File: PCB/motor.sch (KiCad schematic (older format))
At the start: 18 parts, among them J20 70543-0003, U5 TMC2130-TA

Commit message: Change 1k resistors to 4.7k. Update Symbols
Had to update the symbols to the right library again, since
Kicad Nightly changed their library order.

Also changed the 1k resistors to 4.7k to unify resistors and
also upped the PU to a weaker value.
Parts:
- C45, C46, C47, C48, C49, C50, C52, C53: symbol remram-rescue:C-Device -> Device:C
- C51: symbol remram-rescue:CP-Device -> Device:CP
- R37, R38, R39: symbol remram-rescue:R-Device -> Device:R
- TP20, TP21, TP22, TP23: symbol remram-rescue:Test_Point-Connector_Specialized -> Connector:Test_Point

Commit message: Added protection diodes to TMC2130
Diode on IO voltage protects chip to only accept command when
motor voltage is present.

Clamping diodes on motor outputs are for inductive loads.
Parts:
- added D32, D33, D34, D35, D36, D37, D38, D39, D40: S310FA, Diode_SMD:D_SOD-123, symbol Device:D_Schottky
- added R38: 10k, Resistor_SMD:R_0603_1608Metric, symbol Device:R
- renumbered R38 to R39, R39 to R40
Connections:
- net labels added: GND
- wire segments 43 -> 76
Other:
- moved on the sheet: J20, R39

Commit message: Rework the PCB after feedback
This design incooperated following changes:
 * Better power distribution
 * Diodes for driver, endstops and fan tachometer
 * Mounting holes not grounded and size 3.5mm
 * Better EXT3 header description
 * EXT1 and EXT2 footprint for normal 2.54 header
 * Reverse voltage protection for the battery
 * PU for driver enable pin
 * Better crystal placement
 * 2 sided board layout for better routing and
   placement
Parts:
- removed TP20: OA1, TestPoint:TestPoint_Pad_D1.0mm, symbol Connector:Test_Point
- removed TP21: OA2, TestPoint:TestPoint_Pad_D1.0mm, symbol Connector:Test_Point
- removed TP22: OB2, TestPoint:TestPoint_Pad_D1.0mm, symbol Connector:Test_Point
- removed TP23: OB1, TestPoint:TestPoint_Pad_D1.0mm, symbol Connector:Test_Point
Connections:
- wire segments 76 -> 68

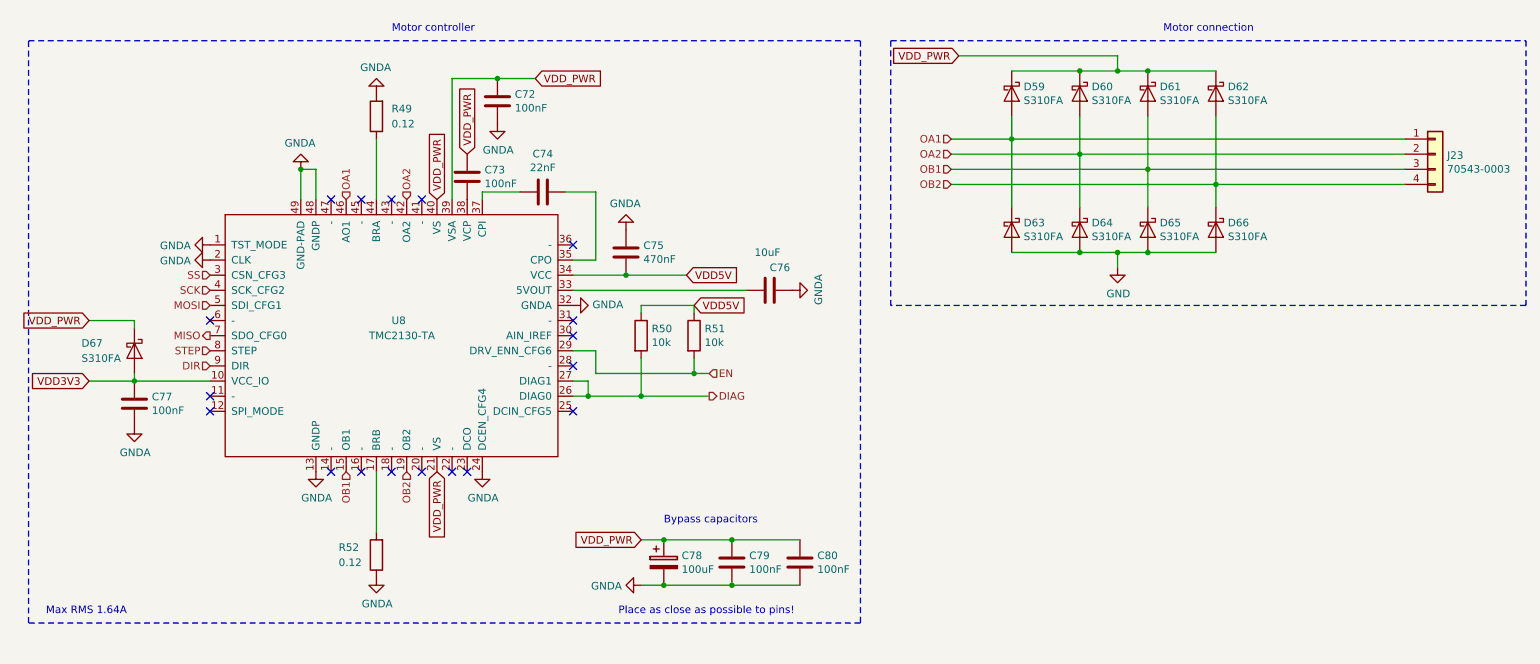
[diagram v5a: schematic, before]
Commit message: Fix PU on FAN RPM, Endstops and Grounding
 * Fixes too weak PU on RPM for fans
 * Simplified endstop setup
 * Grounding fixes:
   * GND below SPI bus
   * 3V3 LDO directly attached
     to main PWR source

Fixes #20
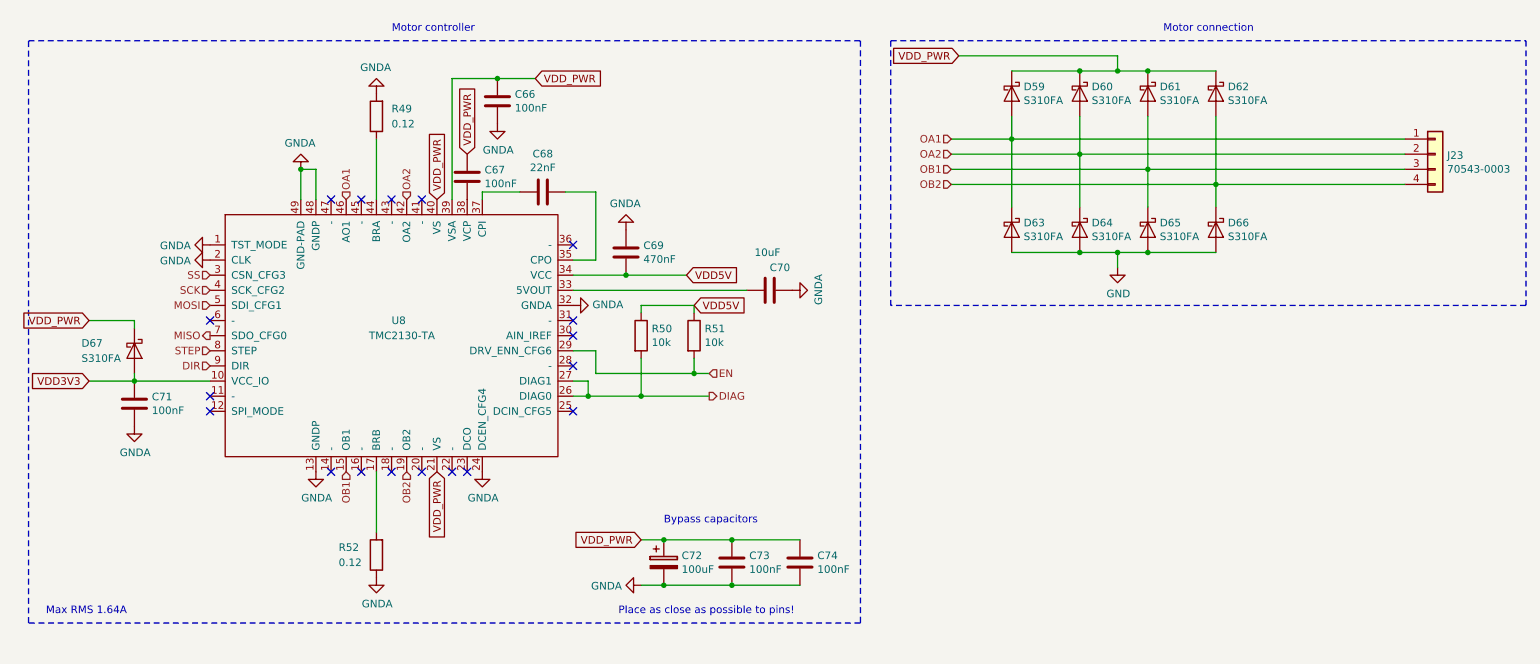
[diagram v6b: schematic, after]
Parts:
- renumbered C45 to C39, C46 to C40, C47 to C41, C48 to C42, C49 to C43, C50 to C44, C51 to C45, C52 to C46, C53 to C47

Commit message: Add a P MOSFET to protect the TPS54308
Since I fried two TPS54308 already, I think it would
be best to implement a reverse voltage protection
before the TPS that provides the 5V rail.

To reuse parts, I also switches the battery protection
P MOSFET to the same part.
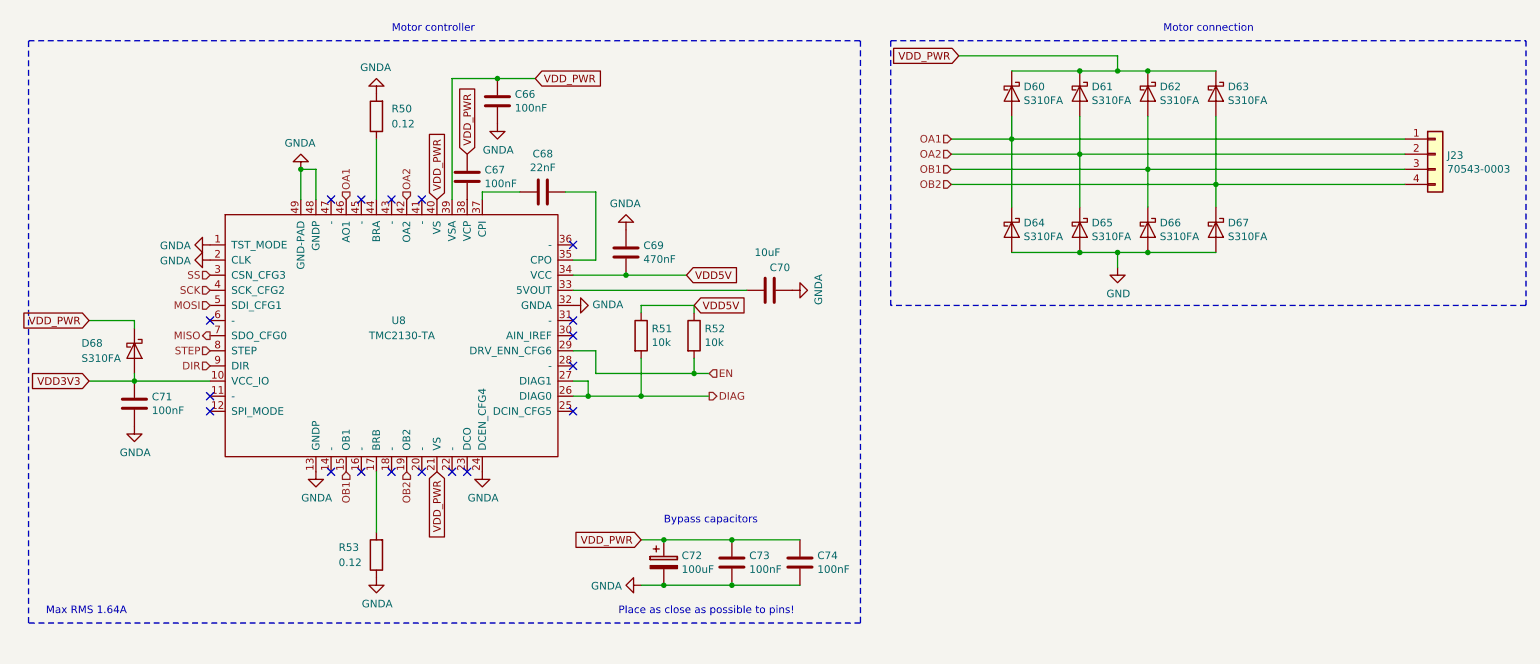
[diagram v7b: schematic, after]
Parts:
- renumbered D32 to D33, D33 to D34, D34 to D35, D35 to D36, D36 to D37, D37 to D38, D38 to D39, D39 to D40, D40 to D41, R37 to R38, R38 to R39, R39 to R40, R40 to R41

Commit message: Add compability for TPS54302
Since the TPS54308 is often not available, we added the
option to also use the TPS54038. This commit added a lot
of components and changed the CSV.
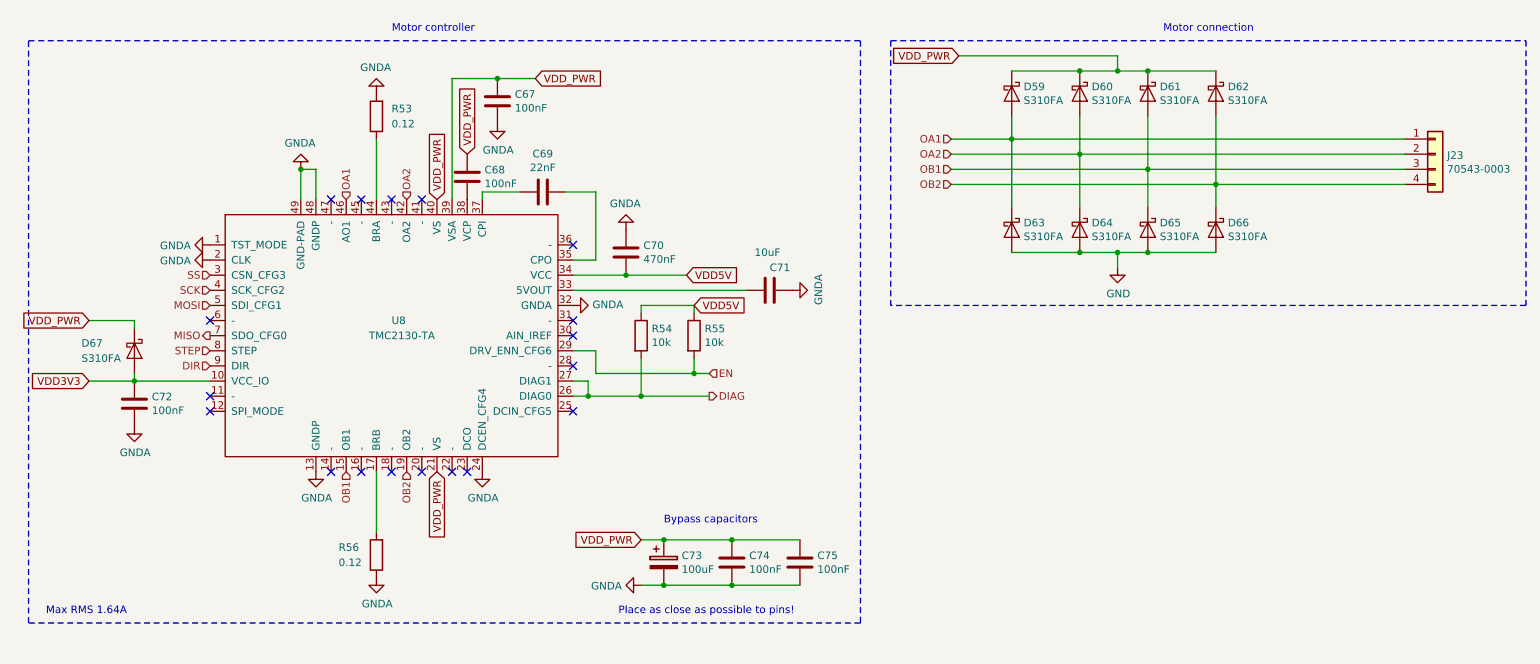
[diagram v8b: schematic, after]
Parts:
- renumbered C39 to C40, C40 to C41, C41 to C42, C42 to C43, C43 to C44, C44 to C45, C45 to C46, C46 to C47, C47 to C48, D33 to D32, D34 to D33, D35 to D34, D36 to D35, D37 to D36, D38 to D37, D39 to D38, D40 to D39, D41 to D40, R38 to R41, R39 to R42, R40 to R43, R41 to R44
